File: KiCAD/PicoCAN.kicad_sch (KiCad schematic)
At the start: 30 parts, among them J1 USB_C_Receptacle_USB2.0_14P, SW1 SW_Push, U1 RP2040, U2 NCP1117-3.3_SOT223, U3 W25Q128JVS, Y1 12 MHz Crystal_GND24

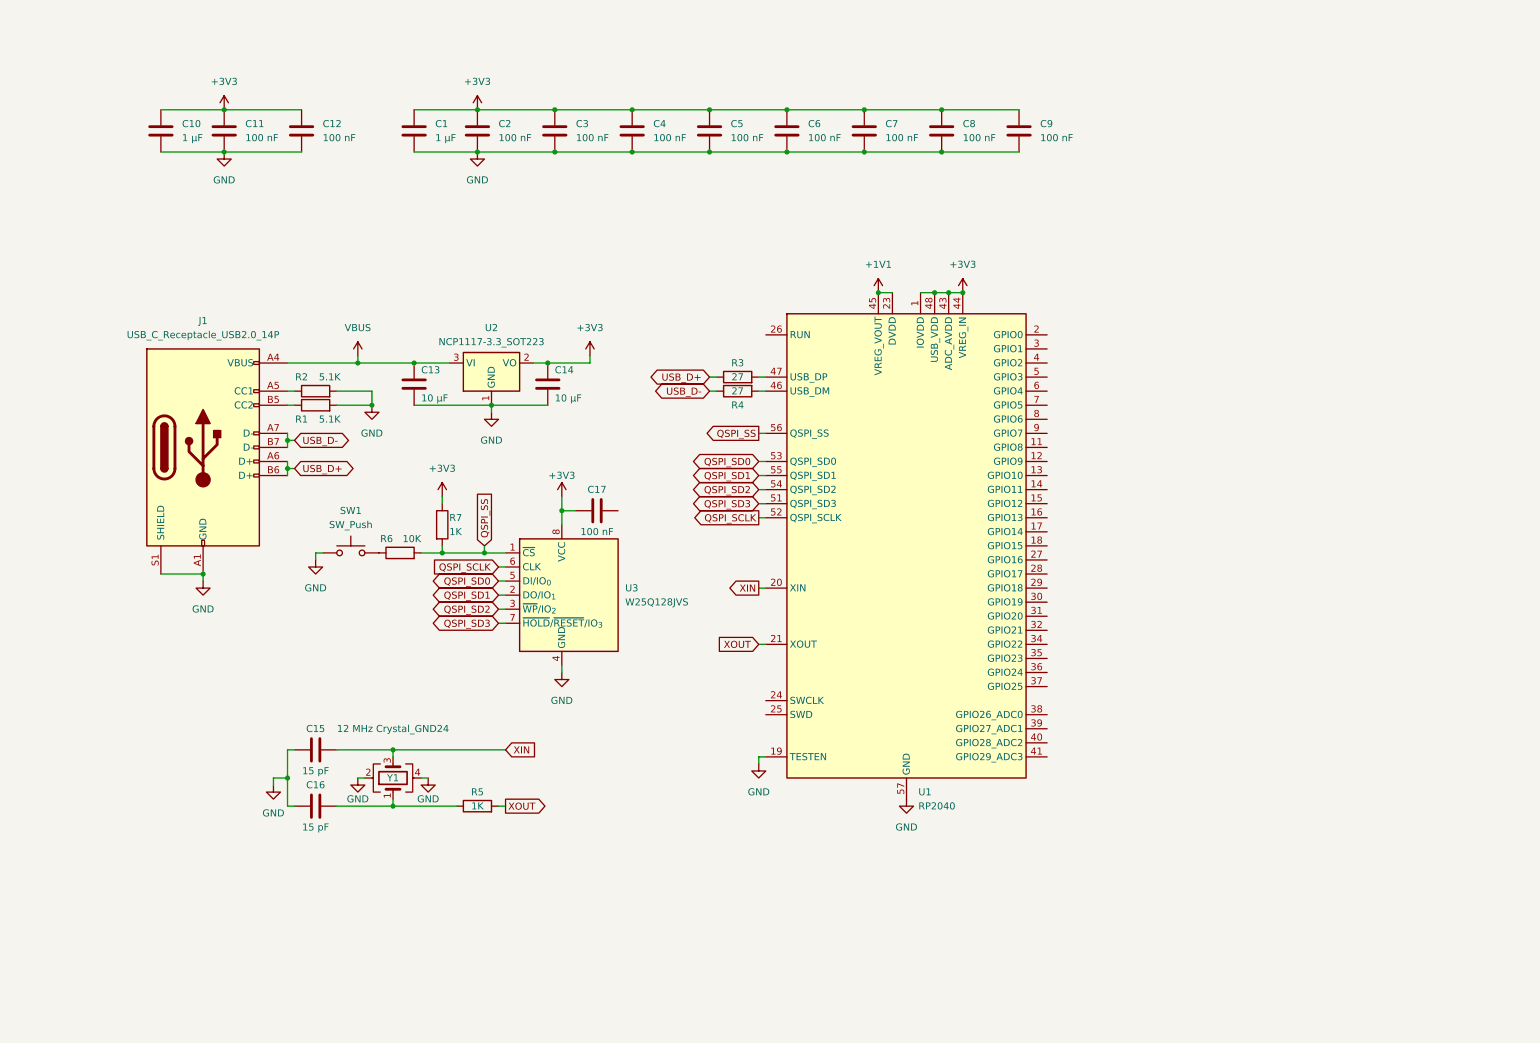
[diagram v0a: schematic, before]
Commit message: Add MCP25625 and more progress
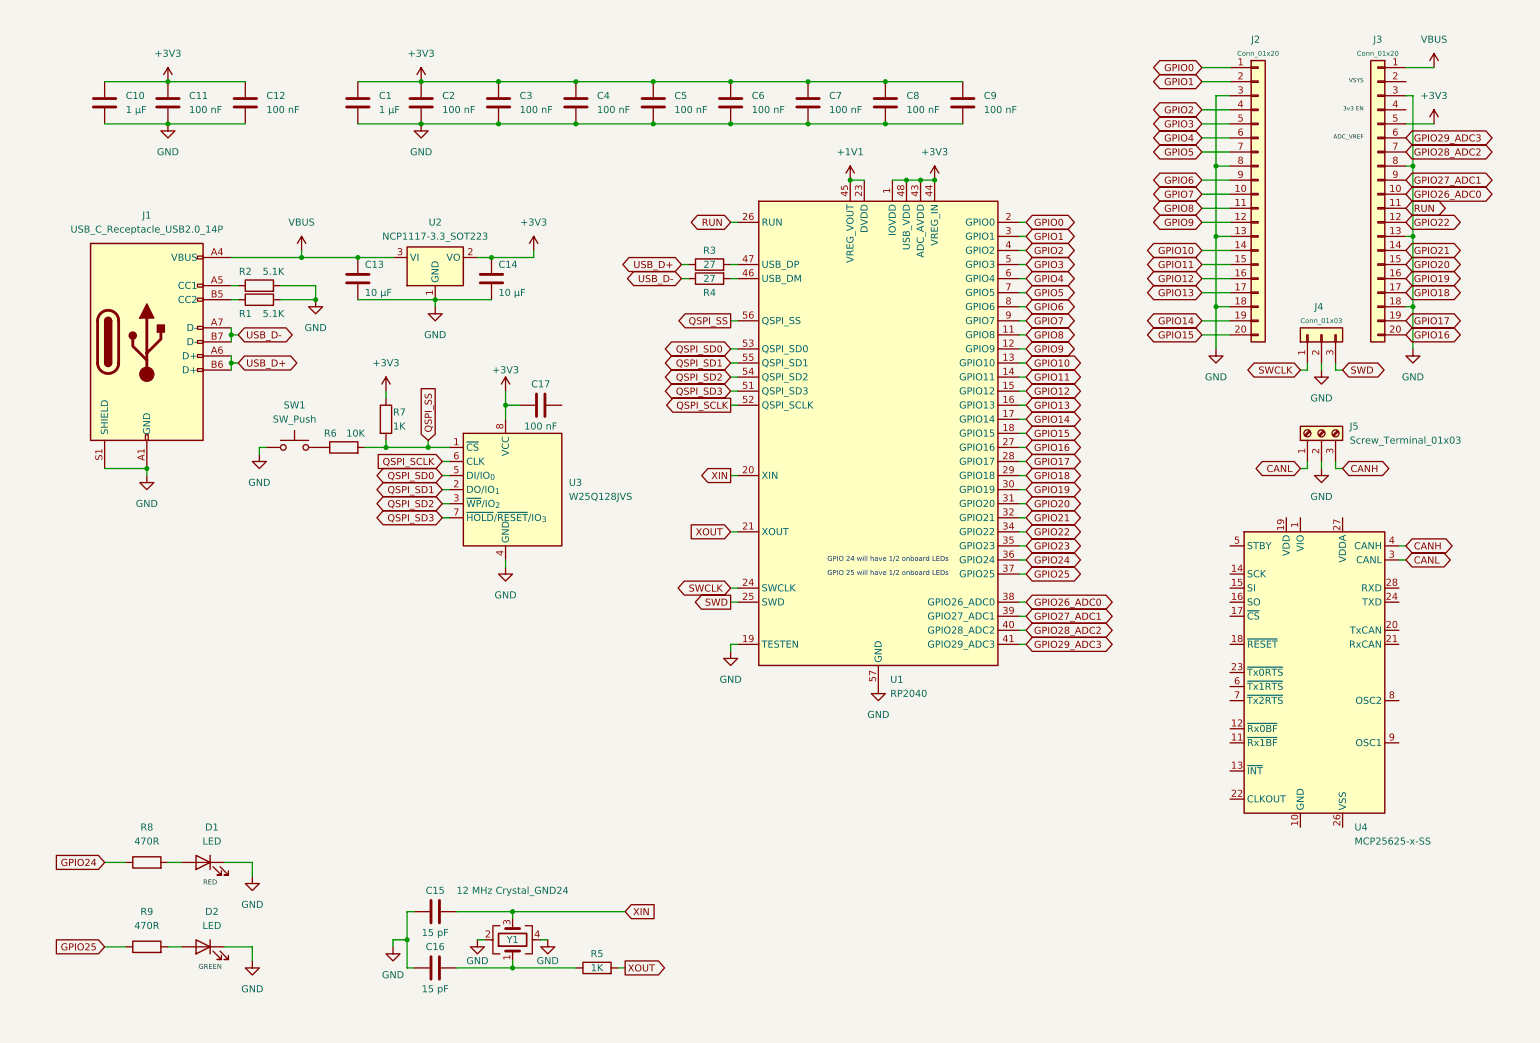
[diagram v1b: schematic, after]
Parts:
- added D1, D2: LED, LED_SMD:LED_0603_1608Metric_Pad1.05x0.95mm_HandSolder, symbol Device:LED
- added J2, J3: Conn_01x20, symbol Connector_Generic:Conn_01x20
- added J4: Conn_01x03, symbol Connector_Generic:Conn_01x03
- added J5: Screw_Terminal_01x03, symbol Connector:Screw_Terminal_01x03
- added R8, R9: 470R, symbol Device:R
- added U4: MCP25625-x-SS, Package_SO:SSOP-28_5.3x10.2mm_P0.65mm, symbol Interface_CAN_LIN:MCP25625-x-SS
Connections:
- net +3V3: now also J3.5 (Pin_5)
- net GND: now also D1.1 (K), D2.1 (K), J2.13 (Pin_13), J2.18 (Pin_18), J2.3 (Pin_3), J2.8 (Pin_8), J3.13 (Pin_13), J3.18 (Pin_18), J3.3 (Pin_3), J3.8 (Pin_8), J4.2 (Pin_2), J5.2 (Pin_2)
- net VBUS: now also J3.1 (Pin_1)
- net GPIO8: now reaches U1.11 (GPIO8)
- net GPIO8: now also J2.11 (Pin_11)
- net GPIO9: now reaches U1.12 (GPIO9)
- net GPIO9: now also J2.12 (Pin_12)
- net GPIO10: now reaches U1.13 (GPIO10)
- net GPIO10: now also J2.14 (Pin_14)
- net GPIO11: now reaches U1.14 (GPIO11)
- net GPIO11: now also J2.15 (Pin_15)
- net GPIO12: now reaches U1.15 (GPIO12)
- net GPIO12: now also J2.16 (Pin_16)
- net GPIO13: now reaches U1.16 (GPIO13)
- net GPIO13: now also J2.17 (Pin_17)
- net GPIO14: now reaches U1.17 (GPIO14)
- net GPIO14: now also J2.19 (Pin_19)
- net GPIO15: now reaches U1.18 (GPIO15)
- net GPIO15: now also J2.20 (Pin_20)
- net GPIO0: now reaches U1.2 (GPIO0)
- net GPIO0: now also J2.1 (Pin_1)
- net SWCLK: now reaches U1.24 (SWCLK)
- net SWCLK: now also J4.1 (Pin_1)
- net SWD: now reaches U1.25 (SWD)
- net SWD: now also J4.3 (Pin_3)
- net RUN: now reaches U1.26 (RUN)
- net RUN: now also J3.11 (Pin_11)
- net GPIO16: now reaches U1.27 (GPIO16)
- net GPIO16: now also J3.20 (Pin_20)
- net GPIO17: now reaches U1.28 (GPIO17)
- net GPIO17: now also J3.19 (Pin_19)
- net GPIO18: now reaches U1.29 (GPIO18)
- net GPIO18: now also J3.17 (Pin_17)
- net GPIO1: now reaches U1.3 (GPIO1)
- net GPIO1: now also J2.2 (Pin_2)
- net GPIO19: now reaches U1.30 (GPIO19)
- net GPIO19: now also J3.16 (Pin_16)
- net GPIO20: now reaches U1.31 (GPIO20)
- net GPIO20: now also J3.15 (Pin_15)
- net GPIO21: now reaches U1.32 (GPIO21)
- net GPIO21: now also J3.14 (Pin_14)
- net GPIO22: now reaches U1.34 (GPIO22)
- net GPIO22: now also J3.12 (Pin_12)
- net GPIO23: now reaches U1.35 (GPIO23)
- net GPIO24: now reaches U1.36 (GPIO24)
- net GPIO24: now also R8.1
- net GPIO25: now reaches U1.37 (GPIO25)
- net GPIO25: now also R9.1
- net GPIO26_ADC0: now reaches U1.38 (GPIO26_ADC0)
- net GPIO26_ADC0: now also J3.10 (Pin_10)
- net GPIO27_ADC1: now reaches U1.39 (GPIO27_ADC1)
- net GPIO27_ADC1: now also J3.9 (Pin_9)
- net GPIO2: now reaches U1.4 (GPIO2)
- net GPIO2: now also J2.4 (Pin_4)
- net GPIO28_ADC2: now reaches U1.40 (GPIO28_ADC2)
- net GPIO28_ADC2: now also J3.7 (Pin_7)
- net GPIO29_ADC3: now reaches U1.41 (GPIO29_ADC3)
- net GPIO29_ADC3: now also J3.6 (Pin_6)
- net GPIO3: now reaches U1.5 (GPIO3)
- net GPIO3: now also J2.5 (Pin_5)
- net GPIO4: now reaches U1.6 (GPIO4)
- net GPIO4: now also J2.6 (Pin_6)
- net GPIO5: now reaches U1.7 (GPIO5)
- net GPIO5: now also J2.7 (Pin_7)
- net GPIO6: now reaches U1.8 (GPIO6)
- net GPIO6: now also J2.9 (Pin_9)
- net GPIO7: now reaches U1.9 (GPIO7)
- net GPIO7: now also J2.10 (Pin_10)
- new net: D2.2 (A), R9.2
- new net: D1.2 (A), R8.2
- new net CANH: J5.3 (Pin_3), U4.4 (CANH)
- new net CANL: J5.1 (Pin_1), U4.3 (CANL)
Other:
- note added: "3v3 EN"
- note added: "ADC_VREF"
- note added: "GPIO 24 will have 1/2 onboard LEDs"
- note added: "GPIO 25 will have 1/2 onboard LEDs"
- note added: "GREEN"
- note added: "RED"
- note added: "VSYS"
- moved on the sheet: C1, C10, C11, C12, C13, C14, C15, C16, C17, C2, C3, C4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

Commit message: Finished MCP25625
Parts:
- added C18, C19: 22 pF, symbol Device:C
- added C20, C21, C22: 100 nF, symbol Device:C
- added J7: Conn_01x02, symbol Connector_Generic:Conn_01x02
- added R10: 120R, symbol Device:R
- added R11: 10K, symbol Device:R
- added Y2: 16 MHz Crystal_GND24, symbol Device:Crystal_GND24
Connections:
- net +3V3: now also U4.1 (VIO), U4.19 (VDD), C20.1, C21.1, C22.1, R11.2
- net CANH: now also R10.2
- net CANL: now also J7.2 (Pin_2)
- net GND: now also C17.1, U4.10 (GND), U4.26 (VSS), U4.5 (STBY), C18.2, C19.2, C20.2, C21.2, C22.2, Y2.2, Y2.4
- net GPIO0: now also U4.16 (SO)
- net GPIO2: now also U4.14 (SCK)
- net GPIO23: now also U4.17 (~{CS})
- net GPIO3: now also U4.15 (SI)
- net at U4.18 (~{RESET}): now also R11.1
- net at U4.20 (TxCAN): now also U4.24 (TXD)
- net at U4.21 (RxCAN): now also U4.28 (RXD)
- net +5V: now reaches U4.27 (VDDA)
- net OSC2: now reaches U4.8 (OSC2)
- net OSC2: now also C19.1, Y2.1
- net OSC1: now reaches U4.9 (OSC1)
- net OSC1: now also C18.1, Y2.3
- new net: J7.1 (Pin_1), R10.1
- no-connect marks 0 -> 7
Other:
- note added: "+ 2 pin jumper shunt"
- note added: "3x 0.1 mF DCCs ->"
- note added: "CAN IC's CS Pin"
- note added: "CAN Termination Resistor"
- note added: "MCP25625"
- note added: "NTS: Check resistor values for LEDs"
- note added: "NTS: Maybe connect INT later?"
- note added: "RP2040"
- moved on the sheet: C1, C10, C11, C12, C15, C16, C2, C3, C4, C5, C6, C7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

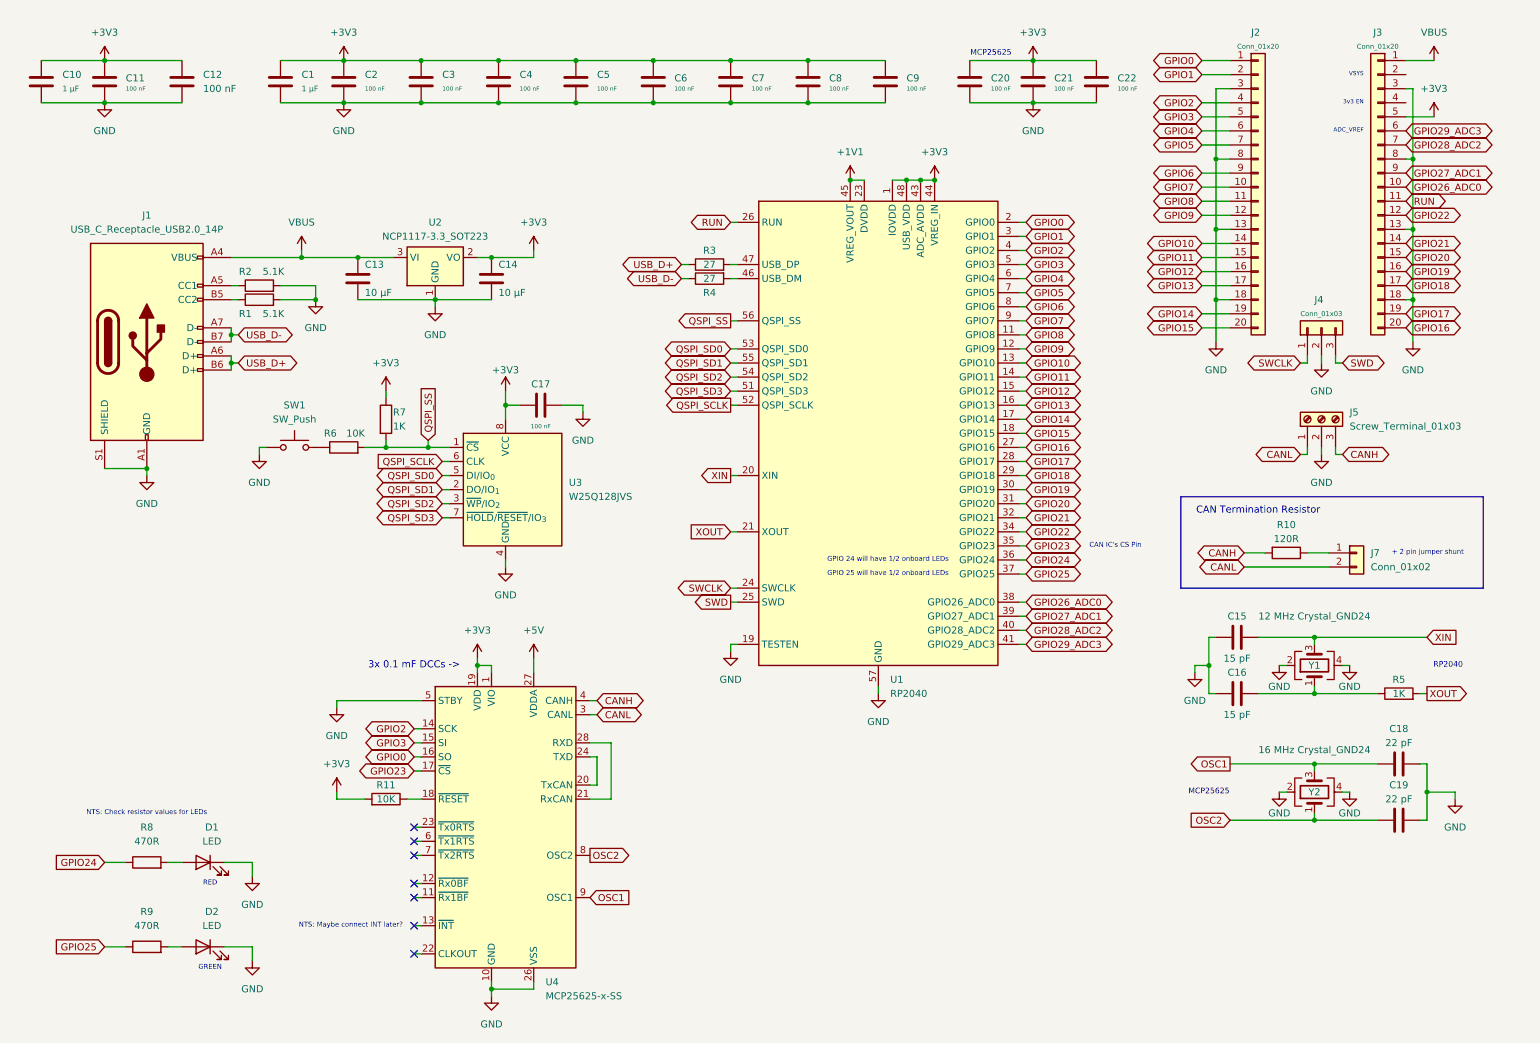
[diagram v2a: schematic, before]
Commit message: Footprints and schematic (w/load caps) finished
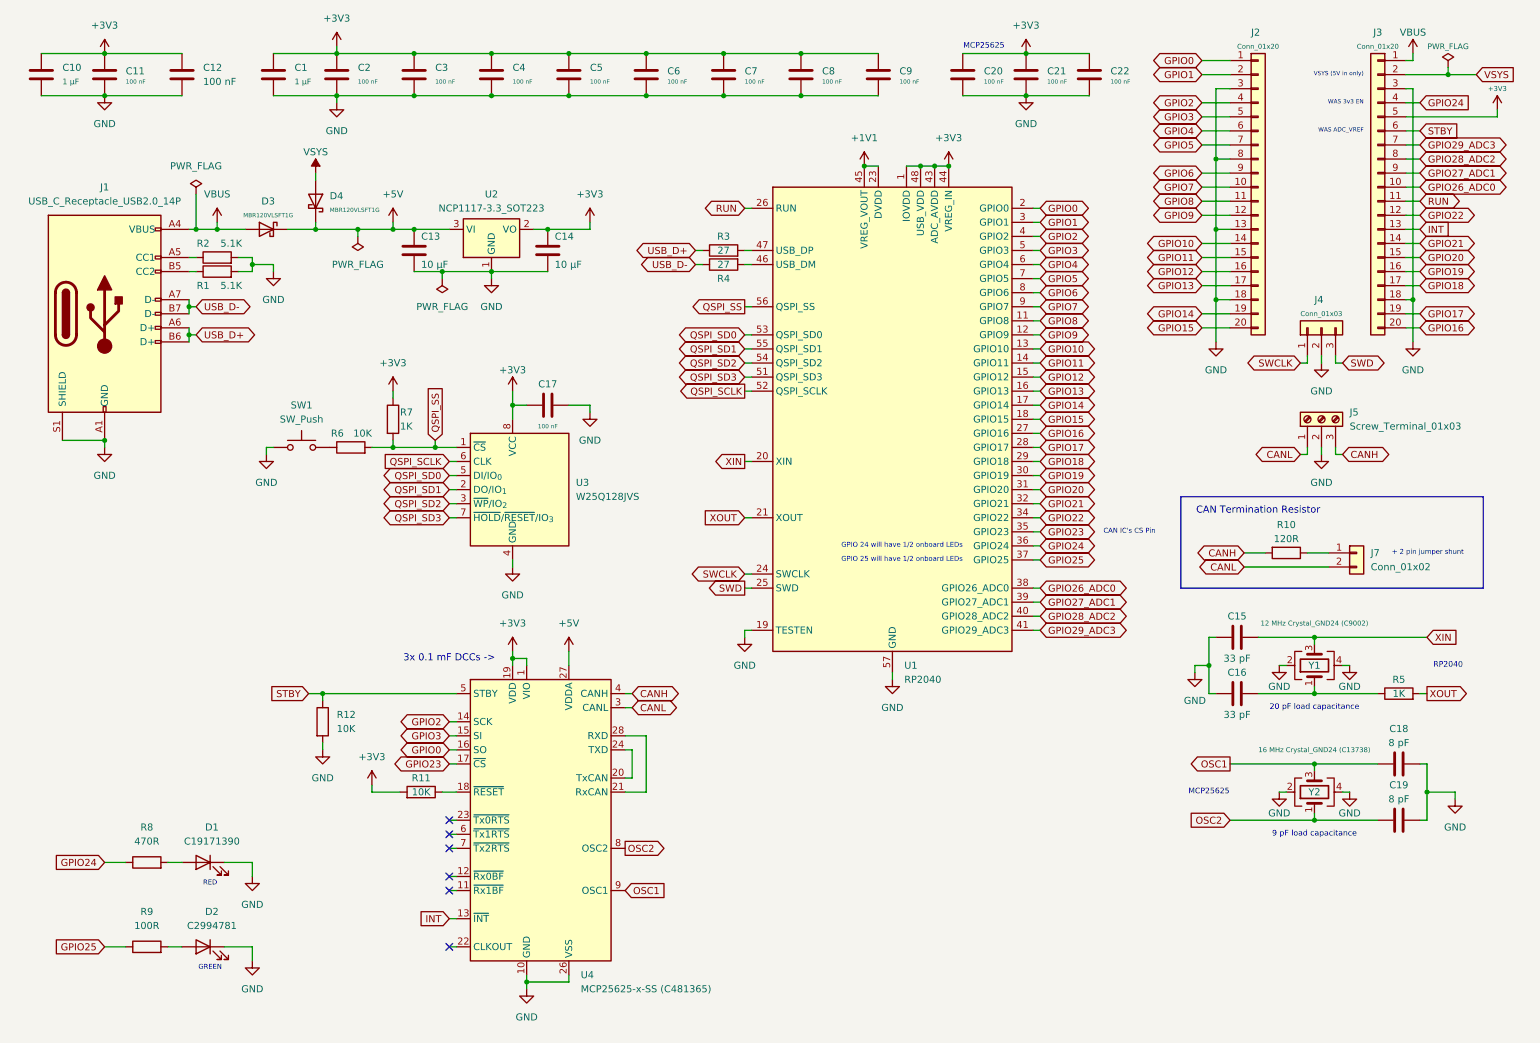
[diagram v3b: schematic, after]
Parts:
- added D3, D4: MBR120VLSFT1G, Diode_SMD:D_SOD-123F, symbol Device:D_Schottky
- added R12: 10K, LED_SMD:LED_0402_1005Metric, symbol Device:R
- C1, C10, C11, C12, C17, C2, C20, C21, C22, C3, C4, C5, C6, C7, C8, C9: footprint (none) -> Capacitor_SMD:C_0402_1005Metric
- C13, C14: footprint (none) -> Capacitor_SMD:C_0603_1608Metric
- C15, C16: value 15 pF -> 33 pF; footprint (none) -> Capacitor_SMD:C_0402_1005Metric
- C18, C19: value 22 pF -> 8 pF; footprint (none) -> Capacitor_SMD:C_0402_1005Metric
- D1: value LED -> C19171390
- D2: value LED -> C2994781
- J1: footprint (none) -> Connector_USB:USB_C_Receptacle_HRO_TYPE-C-31-M-12
- J2, J3: footprint (none) -> Connector_PinHeader_2.54mm:PinHeader_1x20_P2.54mm_Vertical
- J4: footprint (none) -> Connector_PinHeader_2.54mm:PinHeader_1x03_P2.54mm_Vertical
- J5: footprint (none) -> easyeda2kicad:CONN-TH_XY301V-A-5.0-3P
- J7: footprint (none) -> Connector_PinHeader_2.54mm:PinHeader_1x02_P2.54mm_Vertical
- R1, R10, R11, R2, R3, R4, R5, R6, R7, R8: footprint (none) -> LED_SMD:LED_0402_1005Metric
- R9: value 470R -> 100R; footprint (none) -> LED_SMD:LED_0402_1005Metric
- SW1: footprint (none) -> Button_Switch_SMD:SW_Push_SPST_NO_Alps_SKRK
- U4: value MCP25625-x-SS -> MCP25625-x-SS (C481365); footprint Package_SO:SSOP-28_5.3x10.2mm_P0.65mm -> easyeda2kicad:QFN-28_L6.0-W6.0-P0.65-BL-EP
- Y1: value 12 MHz Crystal_GND24 -> 12 MHz Crystal_GND24 (C9002); footprint (none) -> Crystal:Crystal_SMD_3225-4Pin_3.2x2.5mm
- Y2: value 16 MHz Crystal_GND24 -> 16 MHz Crystal_GND24 (C13738); footprint (none) -> Crystal:Crystal_SMD_3225-4Pin_3.2x2.5mm
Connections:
- net +5V: now also C13.1, U2.3 (VI), D3.1 (K), D4.1 (K)
- net GND: now also R12.2; no longer J3.13 (Pin_13), J3.8 (Pin_8), U4.5 (STBY)
- net GPIO24: now also J3.4 (Pin_4)
- net GPIO28_ADC2: now also J3.8 (Pin_8); no longer J3.7 (Pin_7)
- net GPIO29_ADC3: now also J3.7 (Pin_7); no longer J3.6 (Pin_6)
- net VBUS: now also D3.2 (A); no longer C13.1, U2.3 (VI)
- net VSYS: now reaches J3.2 (Pin_2)
- net VSYS: now also D4.2 (A)
- net INT: now reaches U4.13 (~{INT})
- net INT: now also J3.13 (Pin_13)
- new net STBY: J3.6 (Pin_6), R12.1, U4.5 (STBY)
- no-connect marks 7 -> 6
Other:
- note added: "20 pF load capacitance"
- note added: "9 pF load capacitance"
- note added: "VSYS (5V in only)"
- note added: "WAS 3v3 EN"
- note added: "WAS ADC_VREF"
- note removed: "3v3 EN"
- note removed: "ADC_VREF"
- note removed: "NTS: Check resistor values for LEDs"
- note removed: "NTS: Maybe connect INT later?"
- note removed: "VSYS"
- moved on the sheet: C1, C10, C11, C12, C13, C14, C17, C2, C20, C21, C22, C3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

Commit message: PCB Layout
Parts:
- removed J4: Conn_01x03, Connector_PinHeader_2.54mm:PinHeader_1x03_P2.54mm_Vertical, symbol Connector_Generic:Conn_01x03
- removed U2: NCP1117-3.3_SOT223, Package_TO_SOT_SMD:SOT-223-3_TabPin2, symbol Regulator_Linear:NCP1117-3.3_SOT223
- added J4: Conn_01x02, Connector_PinHeader_2.54mm:PinHeader_1x02_P2.54mm_Vertical, symbol Connector_Generic:Conn_01x02
- added U2: MCP1700x-330xxTT, Package_TO_SOT_SMD:SOT-23, symbol Regulator_Linear:MCP1700x-330xxTT
- J5: value Screw_Terminal_01x03 -> Screw_Terminal_01x03 (C3817776); footprint easyeda2kicad:CONN-TH_XY301V-A-5.0-3P -> easyeda2kicad:CONN-TH_3P-P3.50_OSTTE030161
- SW1: footprint Button_Switch_SMD:SW_Push_SPST_NO_Alps_SKRK -> easyeda2kicad:SW-SMD_L3.9-W3.0-P4.45
- U3: value W25Q128JVS -> W25Q16JVUXIQ; footprint Package_SO:SOIC-8_5.3x5.3mm_P1.27mm -> Package_SON:Winbond_USON-8-1EP_3x2mm_P0.5mm_EP0.2x1.6mm
- renumbered R2 to R1, R1 to R2
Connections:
- net +1V1: now also C10.1, C11.1, C12.1
- net +3V3: now also U2.2 (VO); no longer C10.1, C11.1, C12.1
- net +5V: now also U2.3 (VI)
- net GND: now also U2.1 (GND)
- net SWCLK: now also J4.1 (Pin_1)
- net SWD: now also J4.2 (Pin_2)
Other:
- moved on the sheet: J5

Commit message: Finished Traces
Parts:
- added TP1: 5V TestPoint, TestPoint:TestPoint_Pad_1.0x1.0mm, symbol Connector:TestPoint
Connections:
- net +3V3: no longer C22.1
- net +5V: now also C22.1, TP1.1
- net GPIO22: now also J3.11 (Pin_11); no longer J3.12 (Pin_12)
- net RUN: now also J3.12 (Pin_12); no longer J3.11 (Pin_11)
